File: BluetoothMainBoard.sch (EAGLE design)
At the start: 32 parts, among them IC1 MCP73831, J1 J_USB_MICROAB_HIROSE_ZX62-AB-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, U1 MAX921MSA/PR

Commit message: Added the LM386 amplifier to the schematic. Potential problem is the supplu voltage. Considering using two batteries.....?
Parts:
- added C4: 0.1uF, rcl:C-EUC0805
- added U$2, U$3: LM386, Communica:LM386
- R10: value 0k0 -> 10K
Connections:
- removed net N$2: R10.2, U$1.VSENSE
- new net MUTE: U$1.PIO_14
- new net RST: C4.1, R10.1, U$1.RST
- new net SHIIIIIT: U$2.VS
- net 1V8: now also R10.2
- net GND: now also C4.2, U$1.GND2, U$2.GND
- net VBAT: now also U$1.VSENSE; no longer R10.1
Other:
- moved on the sheet: R10
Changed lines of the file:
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@@
 <part name="GND8" library="supply1" deviceset="GND" device=""/>
 <part name="GND9" library="supply1" deviceset="GND" device=""/>
-<part name="R10" library="rcl" deviceset="R-EU_" device="R0805W" value="0k0"/>
 <part name="PWR" library="Communica" deviceset="TACTILE" device=""/>
 <part name="BACK" library="Communica" deviceset="TACTILE" device=""/>
@@
 <part name="PWR_ON" library="Communica" deviceset="TACTILE" device=""/>
 <part name="GND10" library="supply1" deviceset="GND" device=""/>
+<part name="R10" library="rcl" deviceset="R-EU_" device="R0805W" value="10K"/>
+<part name="C4" library="rcl" deviceset="C-EU" device="C0805" value="0.1uF"/>
+<part name="GND11" library="supply1" deviceset="GND" device=""/>
+<part name="GND12" library="supply1" deviceset="GND" device=""/>
+<part name="U$2" library="Communica" deviceset="LM386" device=""/>
+<part name="GND13" library="supply1" deviceset="GND" device=""/>
+<part name="U$3" library="Communica" deviceset="LM386" device=""/>
 </parts>
 <sheets>
@@
 <instance part="GND8" gate="1" x="-66.04" y="81.28"/>
 <instance part="GND9" gate="1" x="30.48" y="83.82"/>
-<instance part="R10" gate="G$1" x="-7.62" y="7.62"/>
 <instance part="PWR" gate="G$1" x="91.44" y="22.86"/>
 <instance part="BACK" gate="G$1" x="104.14" y="22.86"/>
@@
 <instance part="PWR_ON" gate="G$1" x="88.9" y="119.38" rot="R270"/>
 <instance part="GND10" gate="1" x="205.74" y="10.16"/>
+<instance part="R10" gate="G$1" x="-63.5" y="22.86"/>
+<instance part="C4" gate="G$1" x="-76.2" y="15.24"/>
+<instance part="GND11" gate="1" x="-76.2" y="0"/>
+<instance part="GND12" gate="1" x="60.96" y="12.7"/>
+<instance part="U$2" gate="G$1" x="320.04" y="40.64"/>
+<instance part="GND13" gate="1" x="292.1" y="27.94"/>
+<instance part="U$3" gate="G$1" x="320.04" y="76.2"/>
 </instances>
 <busses>
@@
 <label x="157.48" y="33.02" size="1.778" layer="95"/>
 </segment>
+<segment>
+<pinref part="R10" gate="G$1" pin="2"/>
+<wire x1="-58.42" y1="22.86" x2="-48.26" y2="22.86" width="0.1524" layer="91"/>
+<label x="-50.8" y="22.86" size="1.778" layer="95"/>
+</segment>
 </net>
 <net name="VBAT" class="0">
@@
 <label x="-2.54" y="10.16" size="1.778" layer="95"/>
 <wire x1="5.08" y1="10.16" x2="-17.78" y2="10.16" width="0.1524" layer="91"/>
-<pinref part="R10" gate="G$1" pin="1"/>
-<wire x1="-12.7" y1="7.62" x2="-17.78" y2="7.62" width="0.1524" layer="91"/>
 <wire x1="-17.78" y1="7.62" x2="-17.78" y2="10.16" width="0.1524" layer="91"/>
+<pinref part="U$1" gate="G$1" pin="VSENSE"/>
+<wire x1="-17.78" y1="7.62" x2="5.08" y2="7.62" width="0.1524" layer="91"/>
 </segment>
 <segment>
@@
 <wire x1="205.74" y1="12.7" x2="205.74" y2="17.78" width="0.1524" layer="91"/>
 </segment>
+<segment>
+<pinref part="C4" gate="G$1" pin="2"/>
+<wire x1="-76.2" y1="10.16" x2="-76.2" y2="2.54" width="0.1524" layer="91"/>
+<pinref part="GND11" gate="1" pin="GND"/>
+</segment>
+<segment>
+<pinref part="U$1" gate="G$1" pin="GND2"/>
+<pinref part="GND12" gate="1" pin="GND"/>
+<wire x1="45.72" y1="17.78" x2="60.96" y2="17.78" width="0.1524" layer="91"/>
+<wire x1="60.96" y1="17.78" x2="60.96" y2="15.24" width="0.1524" layer="91"/>
+</segment>
+<segment>
+<pinref part="U$2" gate="G$1" pin="GND"/>
+<wire x1="304.8" y1="38.1" x2="292.1" y2="38.1" width="0.1524" layer="91"/>
+<wire x1="292.1" y1="38.1" x2="292.1" y2="30.48" width="0.1524" layer="91"/>
+<pinref part="GND13" gate="1" pin="GND"/>
+</segment>
 </net>
 <net name="N$1" class="0">
@@
 </segment>
 </net>
-<net name="N$2" class="0">
-<segment>
-<pinref part="U$1" gate="G$1" pin="VSENSE"/>
-<wire x1="5.08" y1="7.62" x2="-2.54" y2="7.62" width="0.1524" layer="91"/>
-<pinref part="R10" gate="G$1" pin="2"/>
-</segment>
-</net>
 <net name="N$4" class="0">
 <segment>
@@
 </segment>
 </net>
+<net name="MUTE" class="0">
+<segment>
+<pinref part="U$1" gate="G$1" pin="PIO_14"/>
+<wire x1="5.08" y1="35.56" x2="-2.54" y2="35.56" width="0.1524" layer="91"/>
+<label x="-2.54" y="35.56" size="1.778" layer="95"/>
+</segment>
+</net>
+<net name="RST" class="0">
+<segment>
+<pinref part="U$1" gate="G$1" pin="RST"/>
+<wire x1="5.08" y1="33.02" x2="-2.54" y2="33.02" width="0.1524" layer="91"/>
+<label x="-2.54" y="33.02" size="1.778" layer="95"/>
+</segment>
+<segment>
+<pinref part="C4" gate="G$1" pin="1"/>
+<wire x1="-76.2" y1="17.78" x2="-76.2" y2="22.86" width="0.1524" layer="91"/>
+<pinref part="R10" gate="G$1" pin="1"/>
+<wire x1="-76.2" y1="22.86" x2="-68.58" y2="22.86" width="0.1524" layer="91"/>
+<wire x1="-76.2" y1="22.86" x2="-83.82" y2="22.86" width="0.1524" layer="91"/>
+<junction x="-76.2" y="22.86"/>
+<label x="-83.82" y="22.86" size="1.778" layer="95"/>
+</segment>
+</net>
+<net name="SHIIIIIT" class="0">
+<segment>
+<pinref part="U$2" gate="G$1" pin="VS"/>
+<wire x1="340.36" y1="43.18" x2="358.14" y2="43.18" width="0.1524" layer="91"/>
+<label x="350.52" y="43.18" size="1.778" layer="95"/>
+</segment>
+</net>

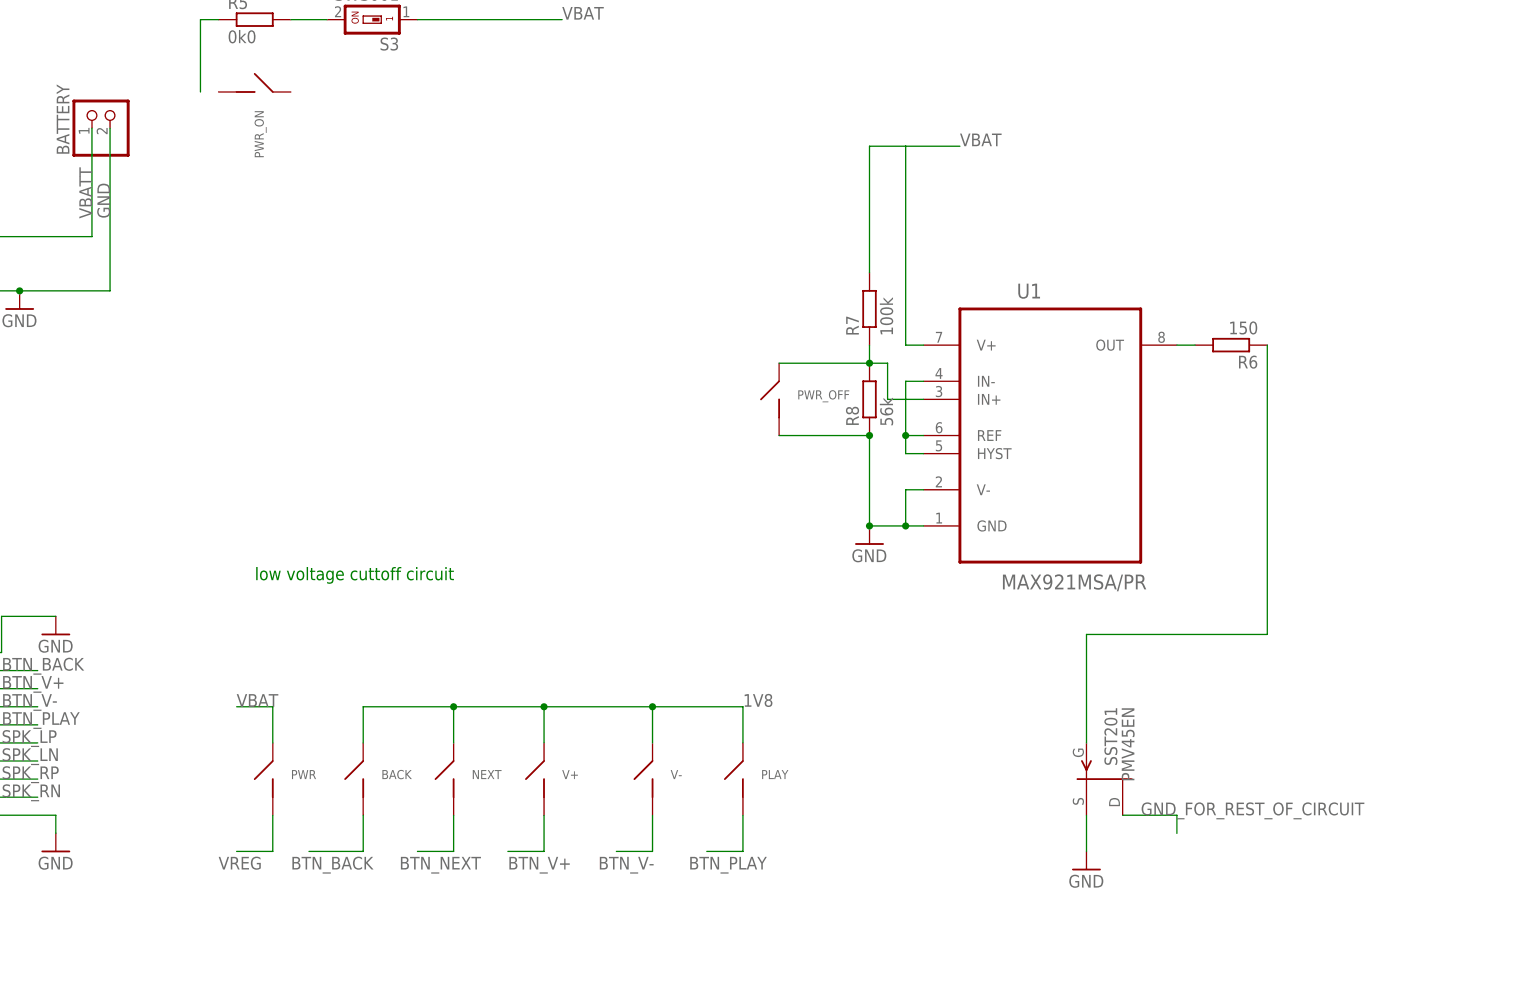
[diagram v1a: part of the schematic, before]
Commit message: added proper relay setup
now usig a pcb solid state relay with an opto isolator built in. Should
have any trouble turning now
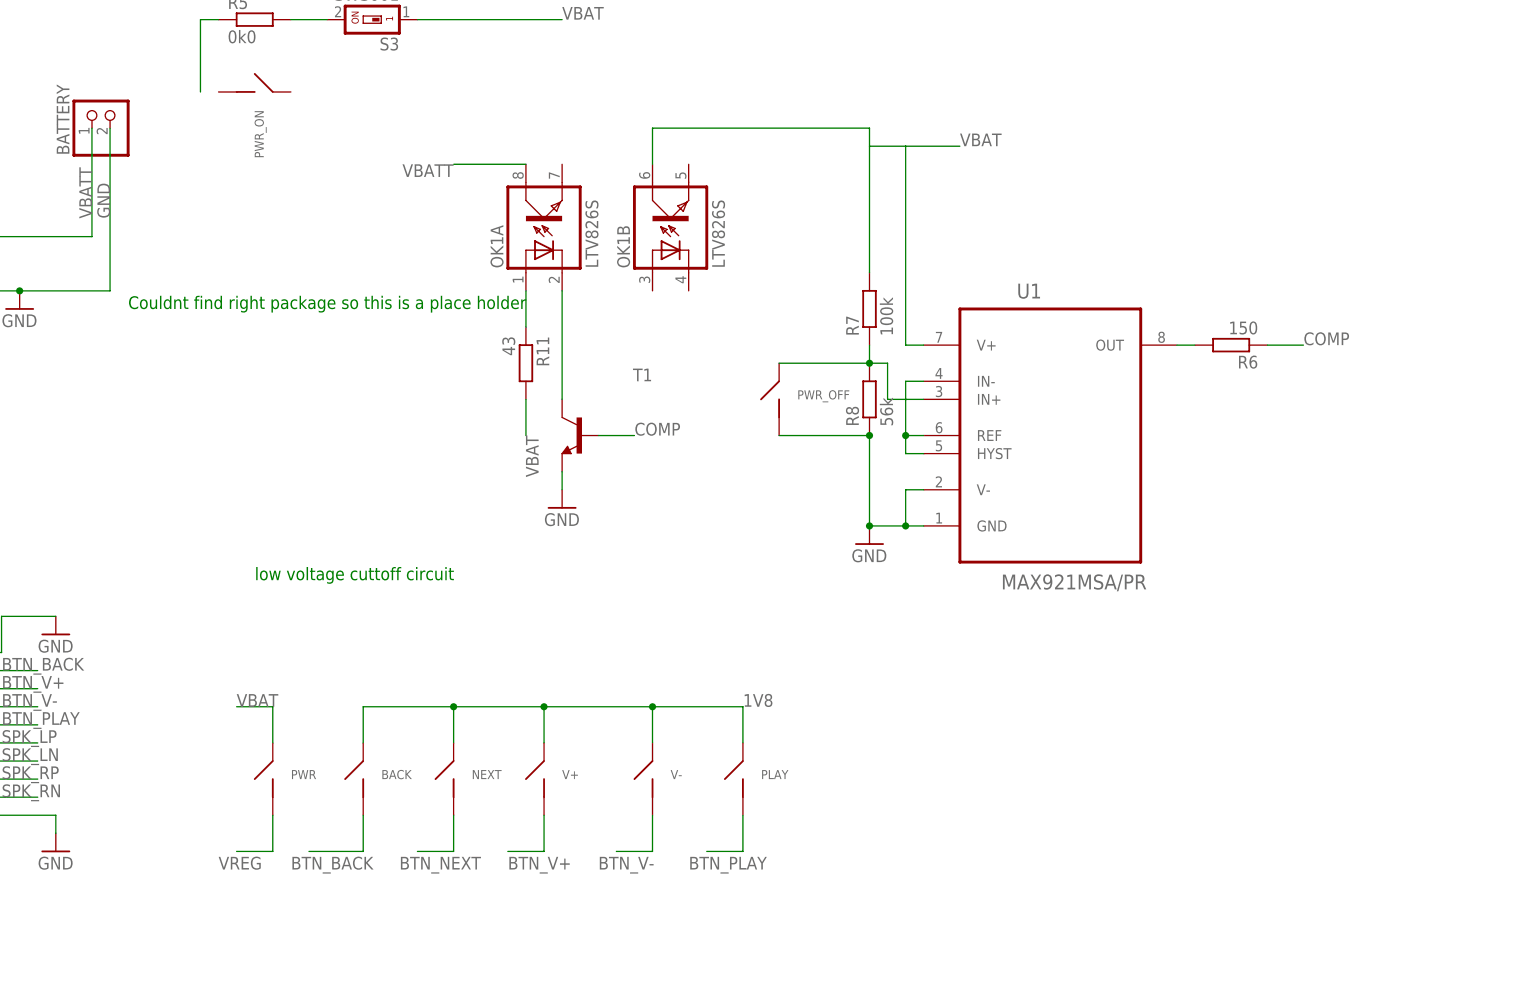
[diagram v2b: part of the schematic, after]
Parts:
- removed PMV45EN: SST201, transistor-fet:SST201
- added OK1: LTV826S, optocoupler:LTV826S
- added R11: 43, rcl:R-EU_R0805W
- added T1: (no value), transistor-neu-to92:BC817-16-NPN-SOT23-BEC
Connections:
- removed net GND_FOR_REST_OF_CIRCUIT: PMV45EN.D
- new net COMP: R6.1, T1.B
- new net N$2: OK1A.A, R11.1
- net GND: now also T1.E; no longer PMV45EN.S
- net N$7: now also OK1A.C, T1.C; no longer PMV45EN.G, R6.1
- net VBAT: now also OK1B.COL, R11.2
- net VBATT: now also OK1A.COL
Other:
- note added: "Couldnt find right package so this is a place holder"
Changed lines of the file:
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@@
 <part name="R5" library="rcl" deviceset="R-EU_" device="R0805W" value="0k0"/>
 <part name="U1" library="Maxim_By_element14_Batch_1" deviceset="MAX921MSA/PR" device=""/>
-<part name="PMV45EN" library="transistor-fet" deviceset="?20*" device="SST" technology="1"/>
 <part name="R6" library="rcl" deviceset="R-EU_" device="R0805W" value="150"/>
 <part name="R7" library="rcl" deviceset="R-EU_" device="R0805W" value="100k"/>
@@
 <part name="PWR_OFF" library="Communica" deviceset="TACTILE" device=""/>
 <part name="PWR_ON" library="Communica" deviceset="TACTILE" device=""/>
-<part name="GND10" library="supply1" deviceset="GND" device=""/>
 <part name="R10" library="rcl" deviceset="R-EU_" device="R0805W" value="10K"/>
 <part name="C4" library="rcl" deviceset="C-EU" device="C0805" value="0.1uF"/>
@@
 <part name="GND13" library="supply1" deviceset="GND" device=""/>
 <part name="U$3" library="Communica" deviceset="LM386" device=""/>
+<part name="OK1" library="optocoupler" deviceset="LTV826" device="S"/>
+<part name="R11" library="rcl" deviceset="R-EU_" device="R0805W" value="43"/>
+<part name="T1" library="transistor-neu-to92" deviceset="*-NPN-" device="SOT23-BEC" technology="BC817-16"/>
+<part name="GND10" library="supply1" deviceset="GND" device=""/>
 </parts>
 <sheets>
@@
 <text x="86.36" y="137.16" size="1.778" layer="91">Cuttoff Cuircuit Bypass</text>
 <text x="-45.72" y="53.34" size="1.778" layer="91">put as close to mosfet as possible</text>
+<text x="71.12" y="88.9" size="1.778" layer="91">Couldnt find right package so this is a place holder</text>
 </plain>
 <instances>
@@
 <instance part="R5" gate="G$1" x="88.9" y="129.54"/>
 <instance part="U1" gate="A" x="200.66" y="73.66"/>
-<instance part="PMV45EN" gate="G$1" x="208.28" y="22.86" rot="R270"/>
 <instance part="R6" gate="G$1" x="226.06" y="83.82" rot="R180"/>
 <instance part="R7" gate="G$1" x="175.26" y="88.9" rot="R90"/>
@@
 <instance part="PWR_OFF" gate="G$1" x="162.56" y="76.2"/>
 <instance part="PWR_ON" gate="G$1" x="88.9" y="119.38" rot="R270"/>
-<instance part="GND10" gate="1" x="205.74" y="10.16"/>
 <instance part="R10" gate="G$1" x="-63.5" y="22.86"/>
 <instance part="C4" gate="G$1" x="-76.2" y="15.24"/>
@@
 <instance part="GND13" gate="1" x="292.1" y="27.94"/>
 <instance part="U$3" gate="G$1" x="320.04" y="76.2"/>
+<instance part="OK1" gate="A" x="129.54" y="101.6" rot="R90"/>
+<instance part="OK1" gate="B" x="147.32" y="101.6" rot="R90"/>
+<instance part="R11" gate="G$1" x="127" y="81.28" rot="R270"/>
+<instance part="T1" gate="G$1" x="134.62" y="71.12" rot="MR0"/>
+<instance part="GND10" gate="1" x="132.08" y="60.96"/>
 </instances>
 <busses>
@@
 <wire x1="180.34" y1="83.82" x2="180.34" y2="111.76" width="0.1524" layer="91"/>
 <wire x1="180.34" y1="111.76" x2="187.96" y2="111.76" width="0.1524" layer="91"/>
+<pinref part="OK1" gate="B" pin="COL"/>
+<wire x1="144.78" y1="109.22" x2="144.78" y2="114.3" width="0.1524" layer="91"/>
+<wire x1="144.78" y1="114.3" x2="175.26" y2="114.3" width="0.1524" layer="91"/>
+<wire x1="175.26" y1="114.3" x2="175.26" y2="111.76" width="0.1524" layer="91"/>
 </segment>
 <segment>
@@
 <wire x1="91.44" y1="33.02" x2="86.36" y2="33.02" width="0.1524" layer="91"/>
 <label x="86.36" y="33.02" size="1.778" layer="95"/>
+</segment>
+<segment>
+<pinref part="R11" gate="G$1" pin="2"/>
+<wire x1="127" y1="76.2" x2="127" y2="71.12" width="0.1524" layer="91"/>
+<label x="127" y="71.12" size="1.778" layer="95" rot="R270"/>
 </segment>
 </net>
@@
 </segment>
 <segment>
-<pinref part="GND10" gate="1" pin="GND"/>
-<pinref part="PMV45EN" gate="G$1" pin="S"/>
-<wire x1="205.74" y1="12.7" x2="205.74" y2="17.78" width="0.1524" layer="91"/>
-</segment>
-<segment>
 <pinref part="C4" gate="G$1" pin="2"/>
 <wire x1="-76.2" y1="10.16" x2="-76.2" y2="2.54" width="0.1524" layer="91"/>
@@
 <wire x1="292.1" y1="38.1" x2="292.1" y2="30.48" width="0.1524" layer="91"/>
 <pinref part="GND13" gate="1" pin="GND"/>
+</segment>
+<segment>
+<pinref part="T1" gate="G$1" pin="E"/>
+<pinref part="GND10" gate="1" pin="GND"/>
+<wire x1="132.08" y1="66.04" x2="132.08" y2="63.5" width="0.1524" layer="91"/>
 </segment>
 </net>
@@
 <label x="66.04" y="101.6" size="1.778" layer="95" rot="R90"/>
 </segment>
+<segment>
+<pinref part="OK1" gate="A" pin="COL"/>
+<wire x1="127" y1="109.22" x2="116.84" y2="109.22" width="0.1524" layer="91"/>
+<label x="116.84" y="109.22" size="1.778" layer="95" rot="R180"/>
+</segment>
 </net>
 <net name="N$5" class="0">
@@
 </segment>
 </net>
-<net name="N$7" class="0">
-<segment>
-<pinref part="R6" gate="G$1" pin="1"/>
-<wire x1="231.14" y1="83.82" x2="231.14" y2="43.18" width="0.1524" layer="91"/>
-<pinref part="PMV45EN" gate="G$1" pin="G"/>
-<wire x1="231.14" y1="43.18" x2="205.74" y2="43.18" width="0.1524" layer="91"/>
-<wire x1="205.74" y1="43.18" x2="205.74" y2="27.94" width="0.1524" layer="91"/>
-</segment>
-</net>
-<net name="GND_FOR_REST_OF_CIRCUIT" class="0">
-<segment>
-<pinref part="PMV45EN" gate="G$1" pin="D"/>
-<wire x1="210.82" y1="17.78" x2="218.44" y2="17.78" width="0.1524" layer="91"/>
-<wire x1="218.44" y1="17.78" x2="218.44" y2="15.24" width="0.1524" layer="91"/>
-<label x="213.36" y="17.78" size="1.778" layer="95"/>
-</segment>
-</net>
 <net name="MUTE" class="0">
 <segment>
@@
 </segment>
 </net>
+<net name="N$2" class="0">
+<segment>
+<pinref part="R11" gate="G$1" pin="1"/>
+<pinref part="OK1" gate="A" pin="A"/>
+<wire x1="127" y1="86.36" x2="127" y2="91.44" width="0.1524" layer="91"/>
+</segment>
+</net>
+<net name="N$7" class="0">
+<segment>
+<pinref part="OK1" gate="A" pin="C"/>
+<wire x1="132.08" y1="91.44" x2="132.08" y2="76.2" width="0.1524" layer="91"/>
+<pinref part="T1" gate="G$1" pin="C"/>
+</segment>
+</net>
+<net name="COMP" class="0">
+<segment>
+<pinref part="T1" gate="G$1" pin="B"/>
+<wire x1="137.16" y1="71.12" x2="142.24" y2="71.12" width="0.1524" layer="91"/>
+<label x="142.24" y="71.12" size="1.778" layer="95"/>
+</segment>
+<segment>
+<pinref part="R6" gate="G$1" pin="1"/>
+<wire x1="231.14" y1="83.82" x2="236.22" y2="83.82" width="0.1524" layer="91"/>
+<label x="236.22" y="83.82" size="1.778" layer="95"/>
+</segment>
+</net>
